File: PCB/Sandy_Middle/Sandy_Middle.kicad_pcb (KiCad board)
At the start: 2 copper layers, 285 x 75.2 mm, 70 parts, among them J1 Conn_02x02_Top_Bottom, J2 Conn_02x02_Top_Bottom, J3 Conn_02x02_Top_Bottom

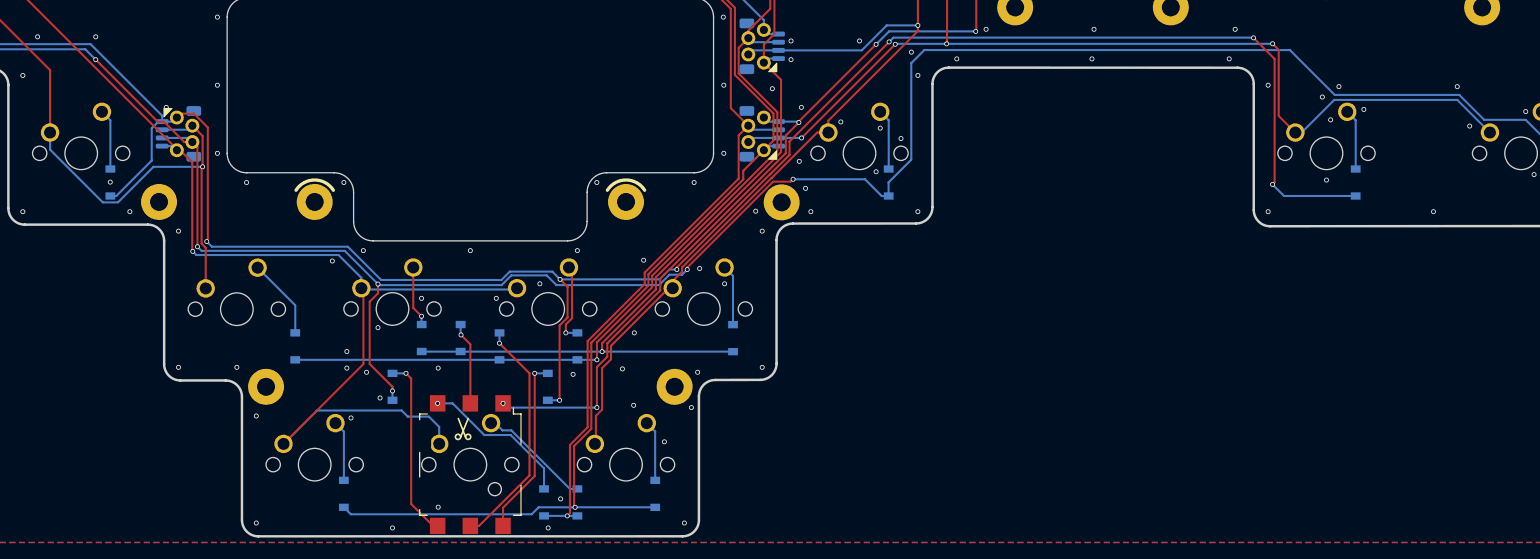
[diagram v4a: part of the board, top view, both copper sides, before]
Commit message: GNDベタ調整
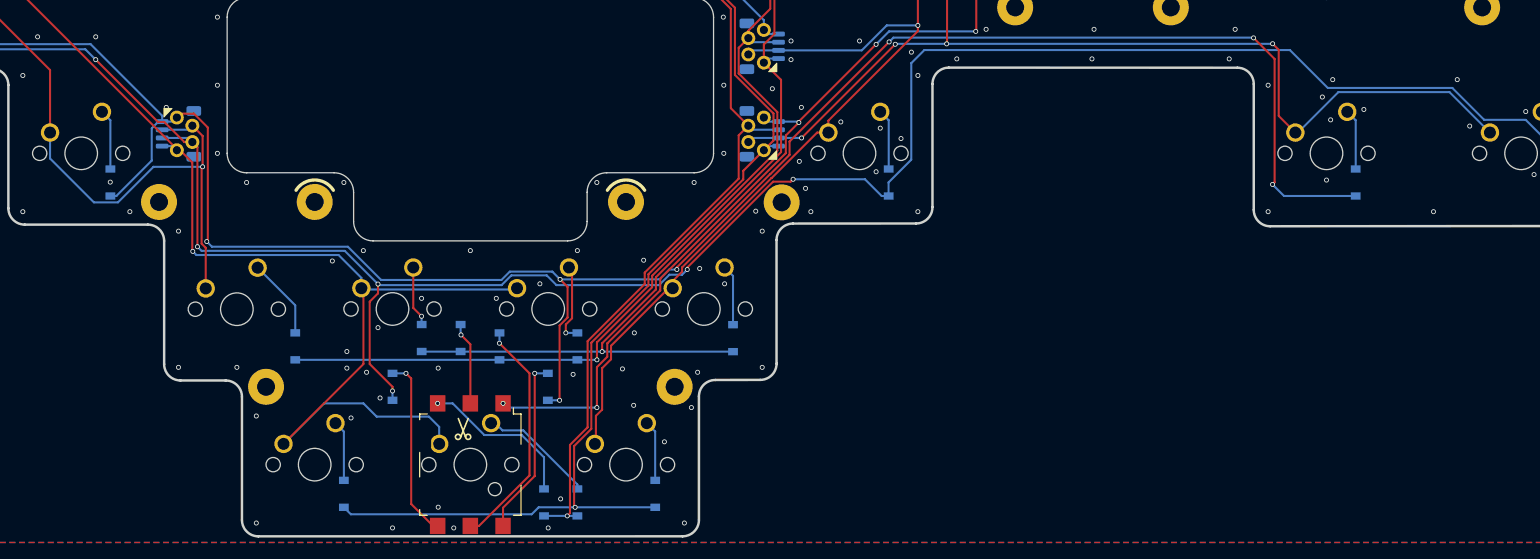
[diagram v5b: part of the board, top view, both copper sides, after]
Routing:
- net Mid_col6: track 119.9 -> 120.7 mm
- net Net-(D17-Pad2): track 18.8 -> 19.6 mm
- net Mid_col3: track 137.2 -> 137.9 mm
- net Mid_col2: track 75.2 -> 75.8 mm
- net Mid_GND: vias 139 -> 140
